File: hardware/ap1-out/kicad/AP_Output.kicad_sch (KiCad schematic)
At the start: 36 parts, among them J1 QWIIC ENTRADA, J2 QWIIC SALIDA, J3 I2C, J4 24V, J5 Q1-Q3, J6 Q4-Q6, J7 Q7 +24 +24, U1 TCA9554PWR, U2 ULN2003ADR

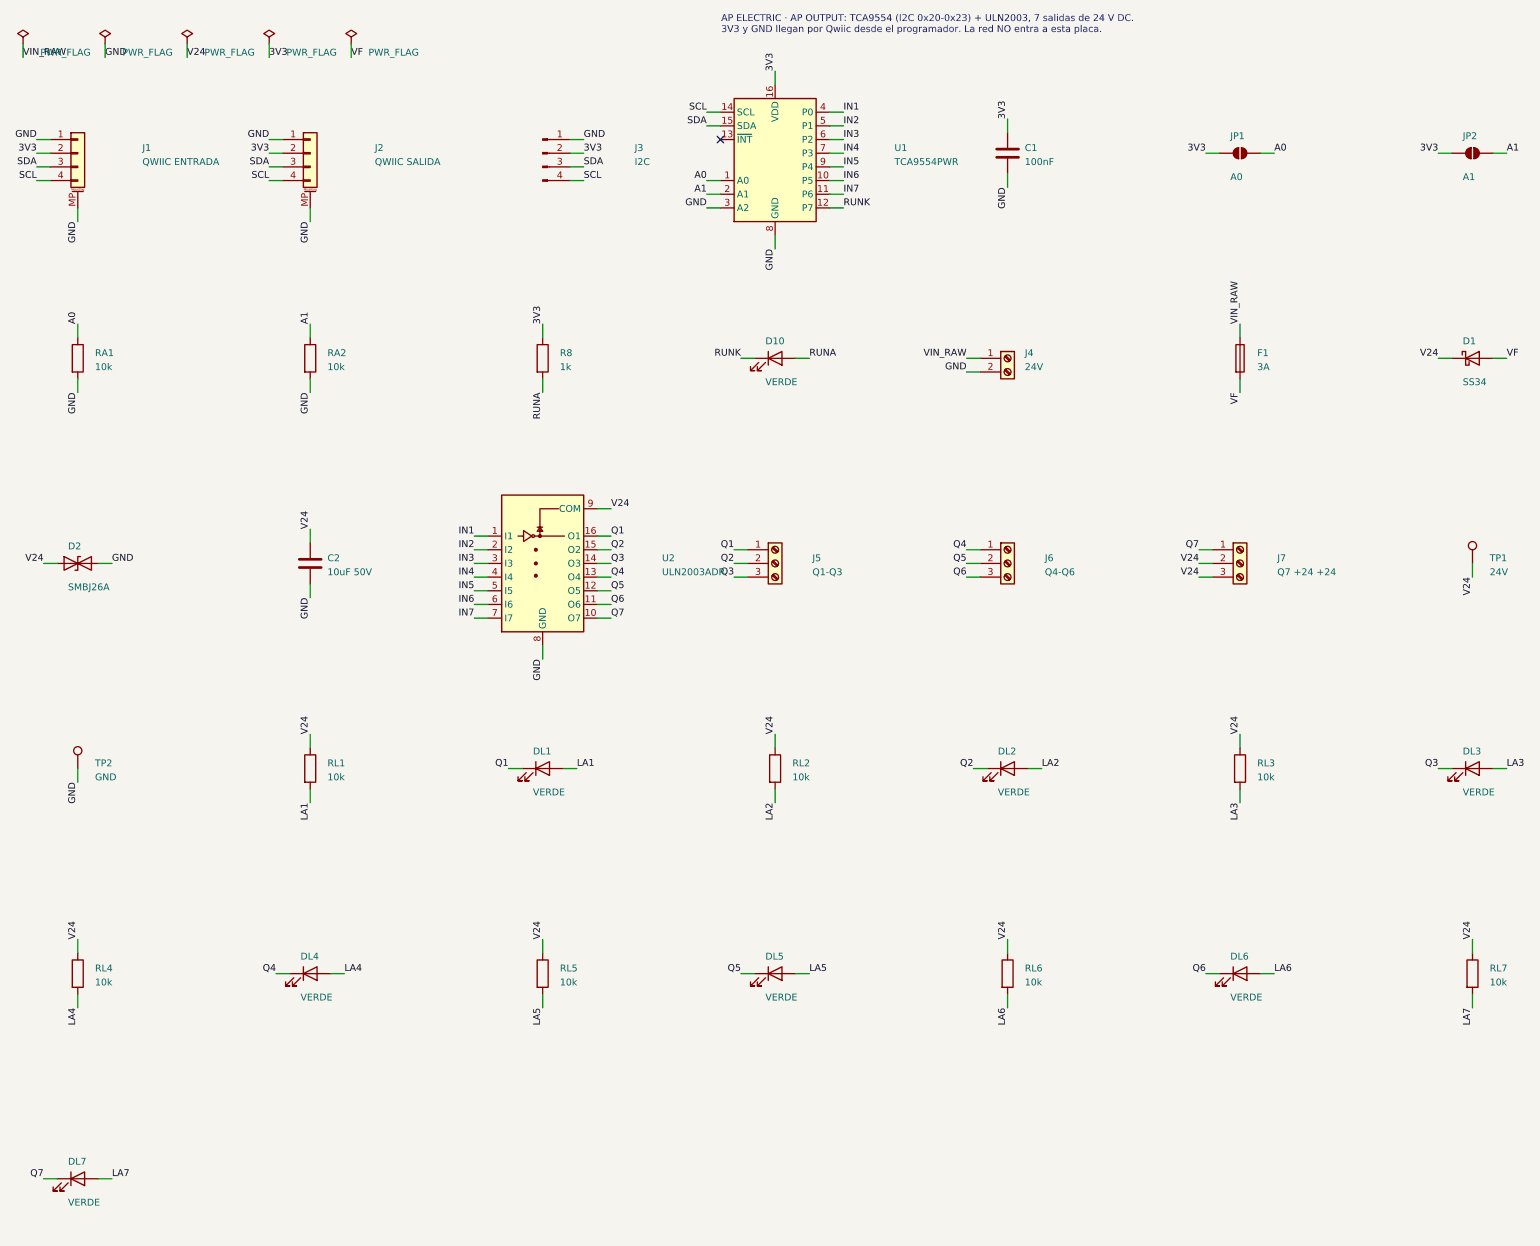
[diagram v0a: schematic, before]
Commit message: AP CONNECT: sin borneras en todas las placas, placa nueva AP PRO AI4 y guía de fabricantes
- Borneras de tornillo reemplazadas por conectores con cable y código LCSC verificado:
  XT60 (C98732), JST VH 2/3/4 (C160315/6/7), JST XH 2/3/4 (C158012, C144394/5), Qwiic
  en BASE, IND, PIX, DMX, PLANTILLA, AP INPUT, AP OUTPUT y DIST 4; zonas de potencia rehechas
- XT60 de la DIST 4 con la polaridad marcada en la huella (pata 1 = -, pata 2 = +)
- TCA9554PWR ya con código (C477924)
- ap1-ai4: 4 entradas 0-10 V / 4-20 mA con ADS1115 (C37593), +24 V para sensores de lazo
- Programa 1.7: lectura AI4, umbrales con acciones, Home Assistant, tarjeta en la app
- FABRICANTES.md: JLCPCB, PCBWay, Seeed, NextPCB, México; impresión 3D y tornillería
- Pedido JLCPCB con 10 placas (AP-0.2 retirada); ERC/DRC/DFM 0 en todas

Co-Authored-By: Claude Opus 5.5 <noreply@anthropic.com>
Claude-Session: https://claude.ai/code/session_01WVk3oGwfQfGTmAT2PMp8oW
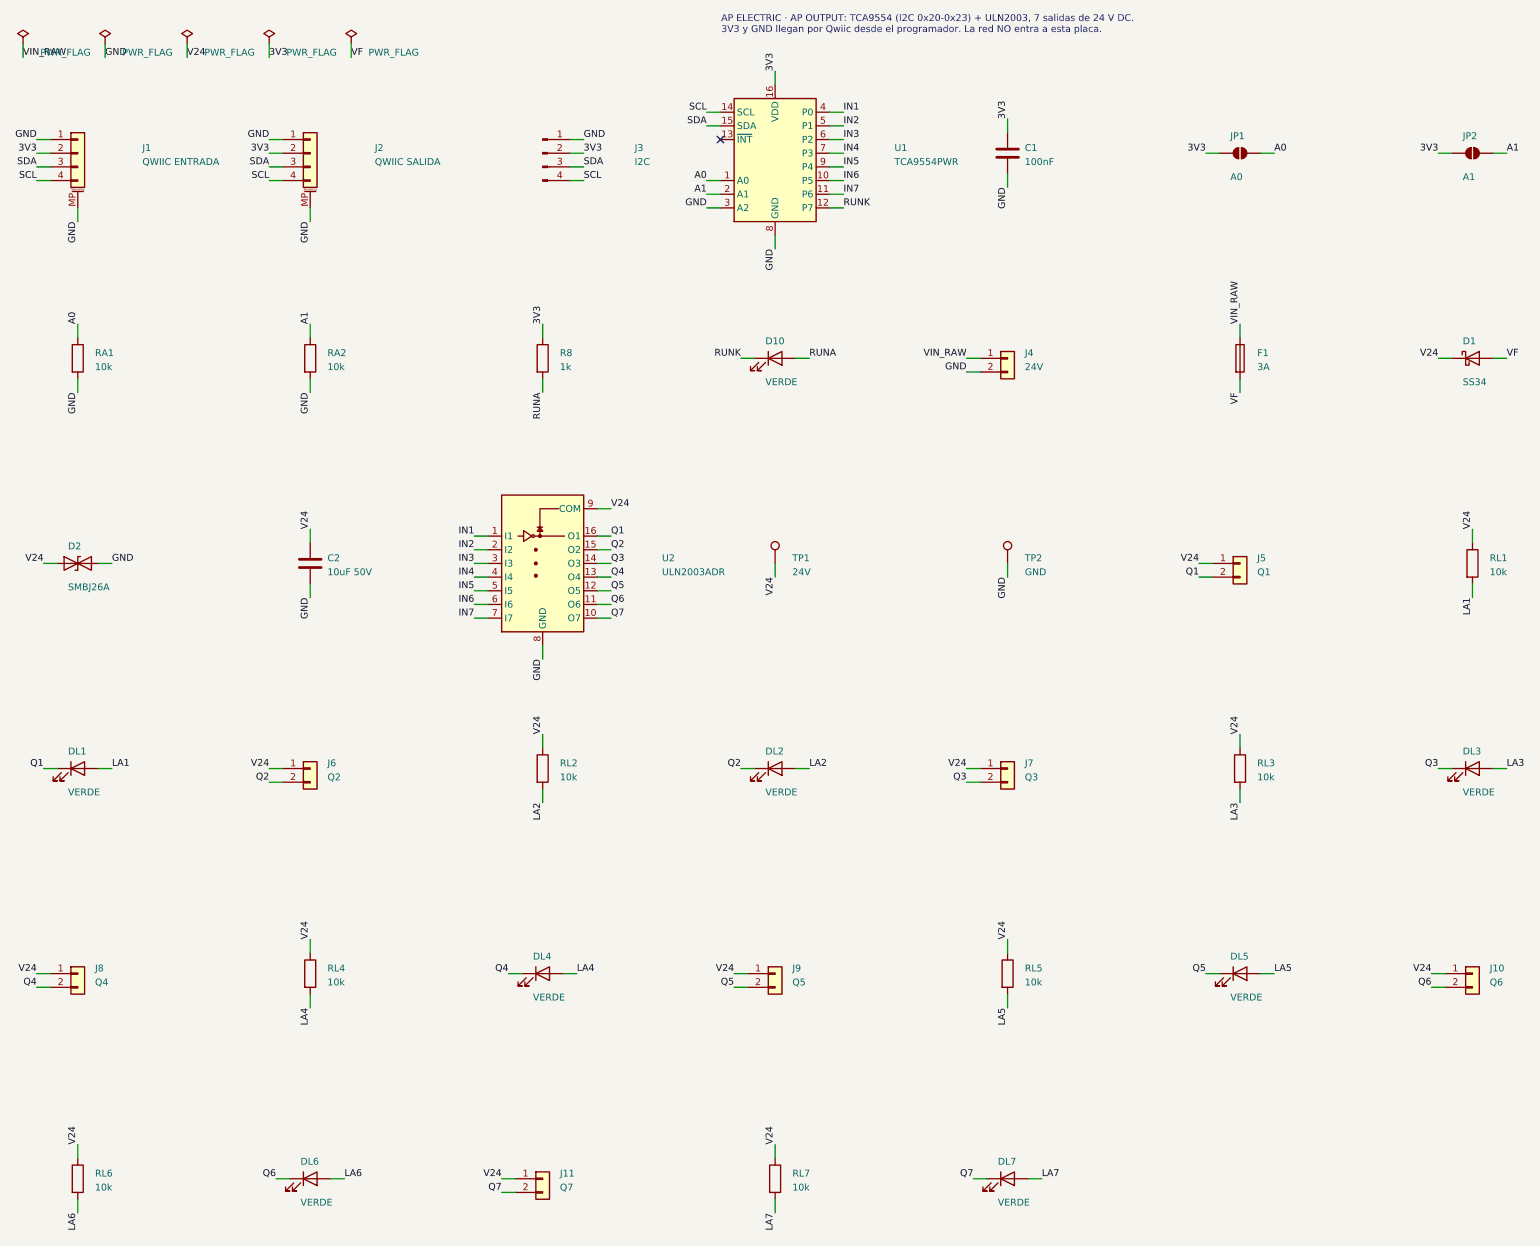
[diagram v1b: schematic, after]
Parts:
- added J10: Q6, Connector_JST:JST_XH_B2B-XH-A_1x02_P2.50mm_Vertical, symbol Connector_Generic:Conn_01x02
- added J11: Q7, Connector_JST:JST_XH_B2B-XH-A_1x02_P2.50mm_Vertical, symbol Connector_Generic:Conn_01x02
- added J8: Q4, Connector_JST:JST_XH_B2B-XH-A_1x02_P2.50mm_Vertical, symbol Connector_Generic:Conn_01x02
- added J9: Q5, Connector_JST:JST_XH_B2B-XH-A_1x02_P2.50mm_Vertical, symbol Connector_Generic:Conn_01x02
- J4: footprint TerminalBlock_Phoenix:TerminalBlock_Phoenix_MKDS-3-2-5.08_1x02_P5.08mm_Horizontal -> Connector_JST:JST_VH_B2P-VH_1x02_P3.96mm_Vertical; symbol Connector:Screw_Terminal_01x02 -> Connector_Generic:Conn_01x02; Funcion Alimentación de las cargas: +24 V y 0 V (la misma fuente qu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 -> Alimentación de las cargas: 1 = +24 V, 2 = 0 V (la misma fu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
- J5: value Q1-Q3 -> Q1; footprint TerminalBlock_Phoenix:TerminalBlock_Phoenix_MKDS-3-3-5.08_1x03_P5.08mm_Horizontal -> Connector_JST:JST_XH_B2B-XH-A_1x02_P2.50mm_Vertical; symbol Connector:Screw_Terminal_01x03 -> Connector_Generic:Conn_01x02; Funcion Salidas 1-3 -> Salida 1: 1 = +24 V, 2 = salida (la carga va entre las dos)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
- J6: value Q4-Q6 -> Q2; footprint TerminalBlock_Phoenix:TerminalBlock_Phoenix_MKDS-3-3-5.08_1x03_P5.08mm_Horizontal -> Connector_JST:JST_XH_B2B-XH-A_1x02_P2.50mm_Vertical; symbol Connector:Screw_Terminal_01x03 -> Connector_Generic:Conn_01x02; Funcion Salidas 4-6 -> Salida 2: 1 = +24 V, 2 = salida (la carga va entre las dos)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
- J7: value Q7 +24 +24 -> Q3; footprint TerminalBlock_Phoenix:TerminalBlock_Phoenix_MKDS-3-3-5.08_1x03_P5.08mm_Horizontal -> Connector_JST:JST_XH_B2B-XH-A_1x02_P2.50mm_Vertical; symbol Connector:Screw_Terminal_01x03 -> Connector_Generic:Conn_01x02; Funcion Salida 7 y +24 V para las cargas -> Salida 3: 1 = +24 V, 2 = salida (la carga va entre las dos)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
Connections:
- net Q1: now also J5.2 (Pin_2); no longer J5.1 (Pin_1)
- net Q2: now also J6.2 (Pin_2); no longer J5.2 (Pin_2)
- net Q3: now also J7.2 (Pin_2); no longer J5.3 (Pin_3)
- net Q4: now also J8.2 (Pin_2); no longer J6.1 (Pin_1)
- net Q5: now also J9.2 (Pin_2); no longer J6.2 (Pin_2)
- net Q6: now also J10.2 (Pin_2); no longer J6.3 (Pin_3)
- net Q7: now also J11.2 (Pin_2); no longer J7.1 (Pin_1)
- net V24: now also J5.1 (Pin_1), J6.1 (Pin_1), J7.1 (Pin_1), J10.1 (Pin_1), J11.1 (Pin_1), J8.1 (Pin_1), J9.1 (Pin_1); no longer J7.2 (Pin_2), J7.3 (Pin_3)
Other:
- moved on the sheet: DL1, DL2, DL4, DL5, DL6, DL7, RL1, RL2, RL4, RL5, RL6, RL7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
